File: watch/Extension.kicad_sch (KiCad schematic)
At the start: 1 part

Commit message: Add speaker
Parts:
- added LS801: Speaker, Same Sky:CMR-12062S-67, symbol Device:Speaker
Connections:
- net GND: now also M801.S113 (GND); no longer M801.S11 (GND)
- net Status: now also M801.S112 (Status); no longer M801.S114 (Status)
- net VHR: now also M801.S12 (+1V8_{HR}); no longer M801.S14 (+1V8_{HR})
- net VSYS: now also M801.S14 (V_{SYS}); no longer M801.S12 (V_{SYS})
- net ~{RESET_{HR}}: now also M801.S114 (~{RESET_{HR}}); no longer M801.S112 (~{RESET_{HR}})
- removed net SP_{N}: M801.S21 (SP_{N})
- removed net SP_{P}: M801.S23 (SP_{P})
- new net: LS801.2, M801.S11 (SP_{N})
- new net: LS801.1, M801.S13 (SP_{P})
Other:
- title: (none) -> Extension
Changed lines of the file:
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@@
 	(paper "A4")
 	(title_block
+		(title "Extension")
 		(date "2025-07-13")
 		(rev "${REVISION}")
@@
 	(wire
 		(pts
+			(xy 172.72 86.36) (xy 184.15 86.36)
+		)
+		(stroke
+			(width 0)
+			(type default)
+		)
+	)
+	(wire
+		(pts
 			(xy 152.4 111.76) (xy 152.4 110.49)
 		)
@@
 	(wire
 		(pts
-			(xy 172.72 86.36) (xy 173.99 86.36)
-		)
-		(stroke
-			(width 0)
-			(type default)
-		)
-	)
-	(wire
-		(pts
 			(xy 128.27 82.55) (xy 129.54 82.55)
 		)
@@
 	(wire
 		(pts
-			(xy 172.72 88.9) (xy 173.99 88.9)
+			(xy 172.72 88.9) (xy 184.15 88.9)
 		)
 		(stroke
@@
 		)
 	)
-	(hierarchical_label "SP_{P}"
-		(shape output)
-		(at 173.99 88.9 0)
-		(effects
-			(font
-				(size 1.27 1.27)
-			)
-			(justify left)
-		)
-	)
 	(hierarchical_label "VHR"
 		(shape input)
 		(at 148.59 63.5 90)
-		(effects
-			(font
-				(size 1.27 1.27)
-			)
-			(justify left)
-		)
-	)
-	(hierarchical_label "SP_{N}"
-		(shape output)
-		(at 173.99 86.36 0)
 		(effects
 			(font
@@
 		(pin "S210"
 		)
-		(pin "S23"
+		(pin "S113"
 		)
 		(pin "S114"
 		)
-		(pin "S21"
+		(pin "S13"
 		)
 		(instances
@@
 					(unit 1)
 				)
+			)
+		)
+	)
+	(symbol
+		(lib_id "Device:Speaker")
+		(at 189.23 86.36 0)
+		(unit 1)
+		(exclude_from_sim no)
+		(in_bom yes)
+		(on_board yes)
+		(dnp no)
+		(fields_autoplaced yes)
+		(property "Reference" "LS801"
+			(at 194.31 86.3599 0)
+			(effects
+				(font
+					(size 1.27 1.27)
+				)
+				(justify left)
+			)
+		)
+		(property "Value" "Speaker"
+			(at 194.31 88.8999 0)
+			(effects
+				(font
+					(size 1.27 1.27)
+				)
+				(justify left)
+			)
+		)
+		(property "Footprint" "Same Sky:CMR-12062S-67"
+			(at 189.23 91.44 0)
+			(effects
+				(font
+					(size 1.27 1.27)
+				)
+				(hide yes)
+			)
+		)
+		(property "Datasheet" "https://www.mouser.de/datasheet/3/6118/1/cmr_12062s_67.pdf"
+			(at 188.976 87.63 0)
+			(effects
+				(font
+					(size 1.27 1.27)
+				)
+				(hide yes)
+			)
+		)
+		(property "Description" "Speaker"
+			(at 189.23 86.36 0)
+			(effects
+				(font
+					(size 1.27 1.27)
+				)
+				(hide yes)
+			)
+		)
+		(property "manf" "Same Sky"
+			(at 189.23 86.36 0)
+			(effects
+				(font
+					(size 1.27 1.27)
+				)
+				(hide yes)
+			)
+		)
+		(property "manf#" "CMR-12062S-67"
+			(at 189.23 86.36 0)
+			(effects
+				(font
+					(size 1.27 1.27)
+				)
+				(hide yes)
+			)
+		)
+		(property "mouser#" "490-CMR-12062S-67"
+			(at 189.23 86.36 0)
+			(effects
+				(font
+					(size 1.27 1.27)
+				)
+				(hide yes)
+			)
+		)
+		(property "CONFIG" ""
+			(at 189.23 86.36 0)
+			(effects
+				(font
+					(size 1.27 1.27)
+				)
+				(hide yes)
+			)
+		)
+		(pin "1"
+		)
+		(pin "2"
+		)
+		(instances
+			(project "ZSWatch-Watch"
+				(path "/d5742f03-3b1a-42e5-a384-018bd4b919aa/c5103ceb-5325-4a84-a025-9638a412984e/ecef31af-e159-4d83-89cb-c5b343e56438"
+					(reference "LS801")
+					(unit 1)
+				)

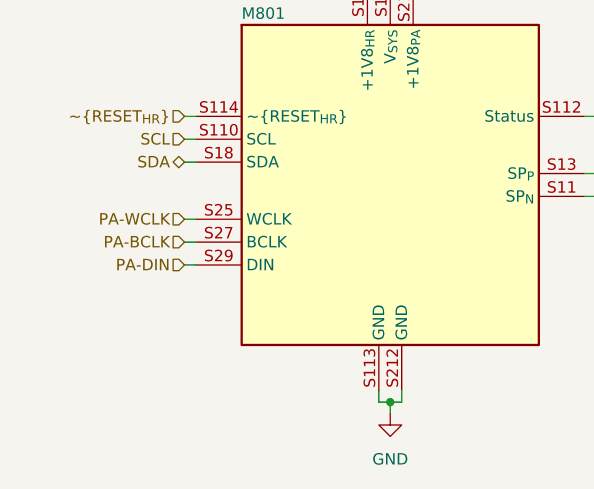
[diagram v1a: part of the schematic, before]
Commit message: Fix wrong Extension footprint
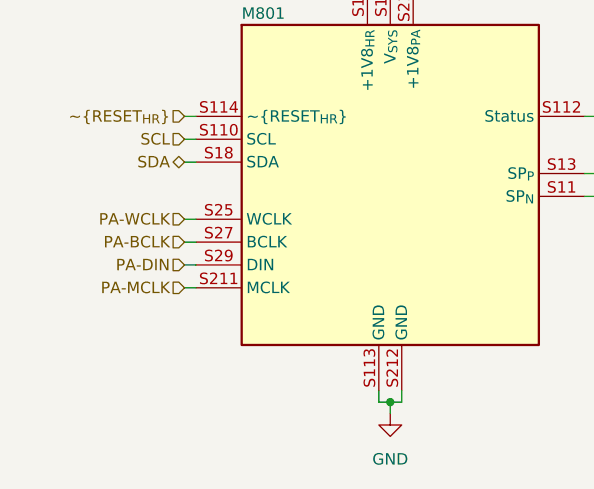
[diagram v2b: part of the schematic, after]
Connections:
- new net PA-MCLK: M801.S211 (MCLK)
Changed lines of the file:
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@@
+	(wire
+		(pts
+			(xy 128.27 99.06) (xy 129.54 99.06)
+		)
+		(stroke
+			(width 0)
+			(type default)
+		)
+	)
 	(wire
 		(pts
@@
 			(width 0)
 			(type default)
+		)
+	)
+	(hierarchical_label "PA-MCLK"
+		(shape input)
+		(at 128.27 99.06 180)
+		(effects
+			(font
+				(size 1.27 1.27)
+			)
+			(justify right)
 		)
 	)
@@
 		(pin "S13"
 		)
+		(pin "S211"
+		)
 		(instances

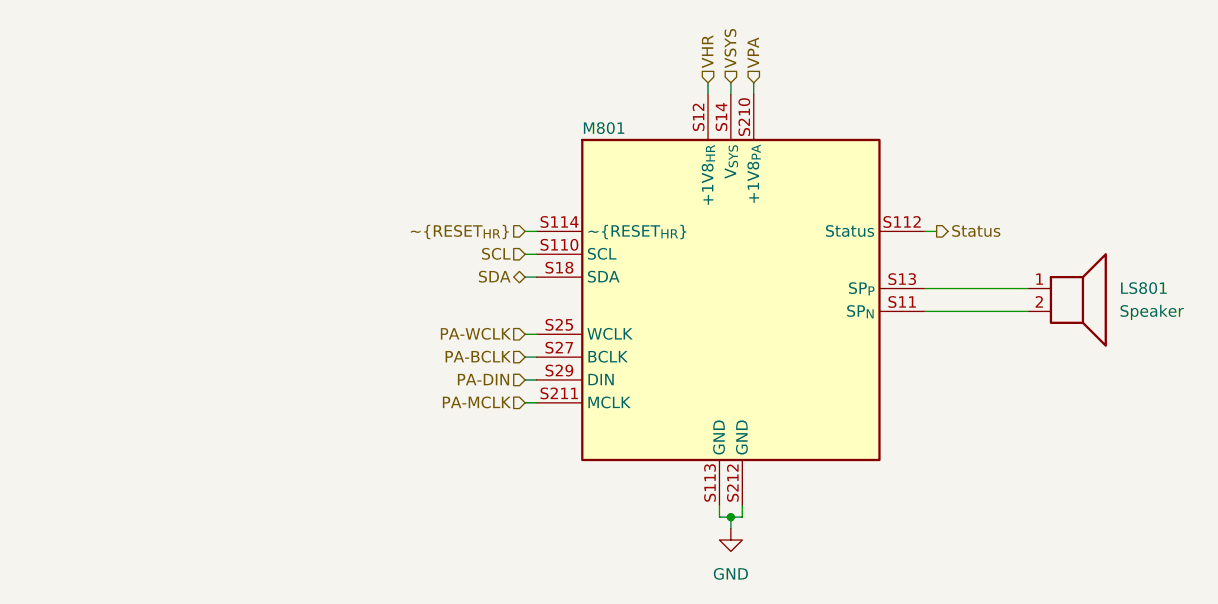
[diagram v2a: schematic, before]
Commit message: New battery connector
- Add CI/CD workflow to check for changelog updates on pull requests

Signed-off-by: Daniel Kampert <DanielKampert|kampis-elektroecke.de>
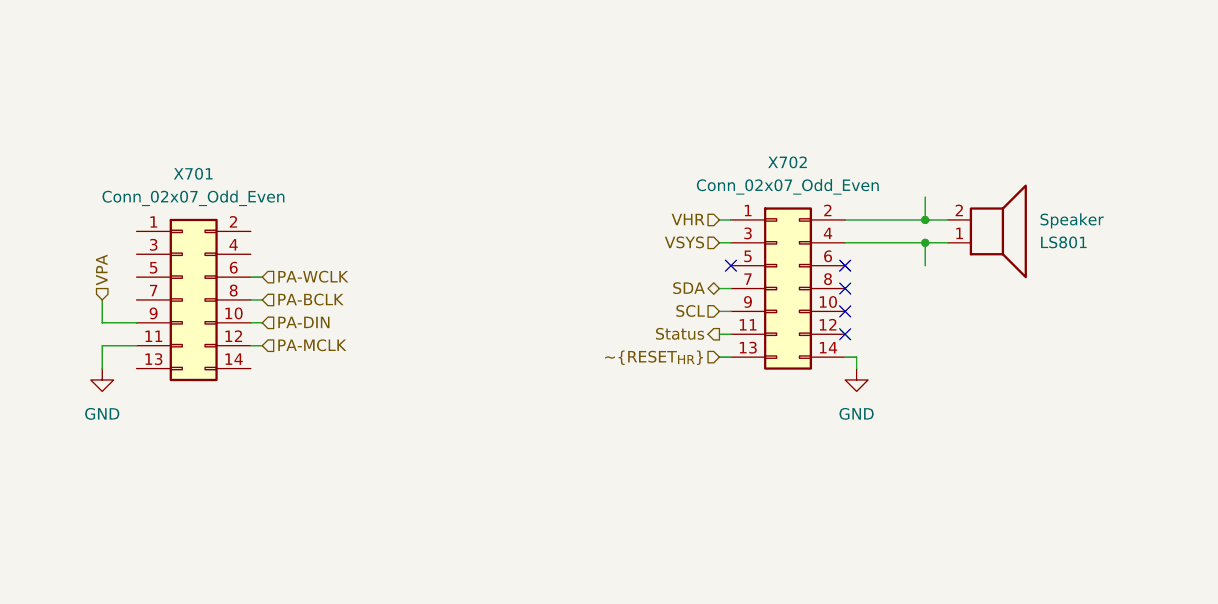
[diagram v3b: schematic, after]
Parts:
- removed M801: ~, ZSWatch:Extension, symbol ZSWatch:Extension
- added X701, X702: Conn_02x07_Odd_Even, Amphenol:101P014FB110, symbol Connector_Generic:Conn_02x07_Odd_Even
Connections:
- net GND: now also X701.11 (Pin_11), X702.14 (Pin_14)
- net PA-BCLK: now also X701.8 (Pin_8)
- net PA-DIN: now also X701.10 (Pin_10)
- net PA-MCLK: now also X701.12 (Pin_12)
- net PA-WCLK: now also X701.6 (Pin_6)
- net SCL: now also X702.9 (Pin_9)
- net SDA: now also X702.7 (Pin_7)
- net Status: now also X702.11 (Pin_11)
- net VHR: now also X702.1 (Pin_1)
- net VPA: now also X701.9 (Pin_9)
- net VSYS: now also X702.3 (Pin_3)
- net ~{RESET_{HR}}: now also X702.13 (Pin_13)
- net at LS801.2: now also X702.2 (Pin_2)
- net at LS801.1: now also X702.4 (Pin_4)
- no-connect marks 0 -> 5
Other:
- moved on the sheet: LS801

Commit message: Replace wrong extension connectors
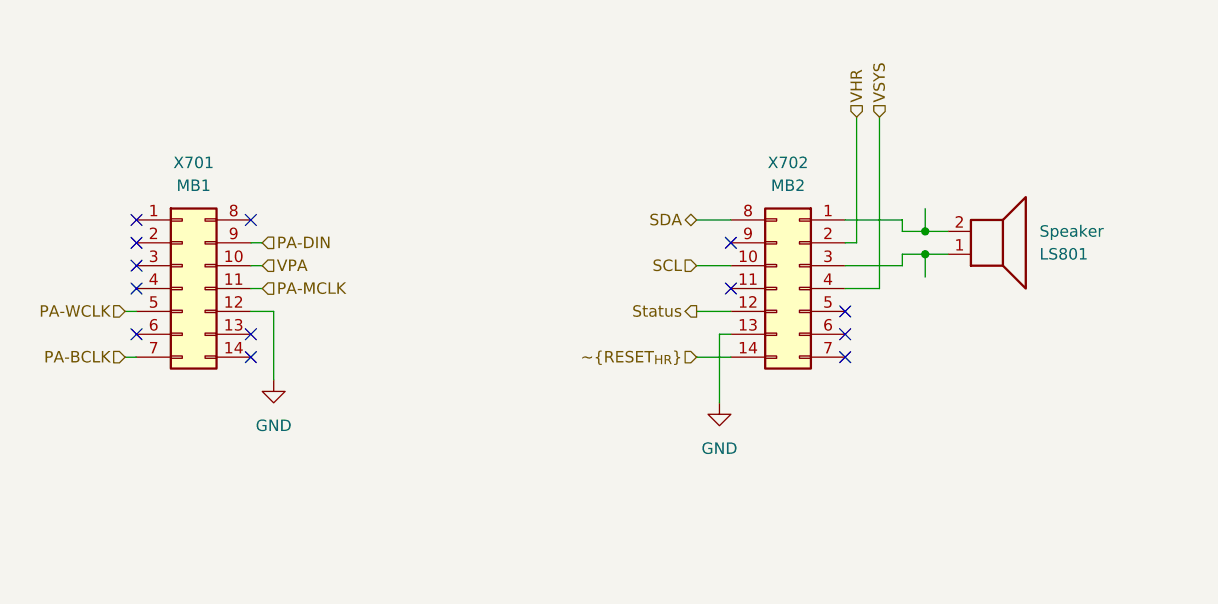
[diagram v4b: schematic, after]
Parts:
- X701: value Conn_02x07_Odd_Even -> MB1; footprint Amphenol:101P014FB110 -> Amphenol:101R014FB110; symbol Connector_Generic:Conn_02x07_Odd_Even -> Connector_Generic:Conn_02x07_Top_Bottom; manf (none) -> Amphenol Aorora; manf# (none) -> 101R014FB110; mouser# (none) -> 649-101R014FB110
- X702: value Conn_02x07_Odd_Even -> MB2; footprint Amphenol:101P014FB110 -> Amphenol:101R014FB110; symbol Connector_Generic:Conn_02x07_Odd_Even -> Connector_Generic:Conn_02x07_Top_Bottom; manf (none) -> Amphenol Aorora; manf# (none) -> 101R014FB110; mouser# (none) -> 649-101R014FB110
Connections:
- net GND: now also X701.12 (Pin_12), X702.13 (Pin_13); no longer X701.11 (Pin_11), X702.14 (Pin_14)
- net PA-BCLK: now also X701.7 (Pin_7); no longer X701.8 (Pin_8)
- net PA-DIN: now also X701.9 (Pin_9); no longer X701.10 (Pin_10)
- net PA-MCLK: now also X701.11 (Pin_11); no longer X701.12 (Pin_12)
- net PA-WCLK: now also X701.5 (Pin_5); no longer X701.6 (Pin_6)
- net SCL: now also X702.10 (Pin_10); no longer X702.9 (Pin_9)
- net SDA: now also X702.8 (Pin_8); no longer X702.7 (Pin_7)
- net Status: now also X702.12 (Pin_12); no longer X702.11 (Pin_11)
- net VHR: now also X702.2 (Pin_2); no longer X702.1 (Pin_1)
- net VPA: now also X701.10 (Pin_10); no longer X701.9 (Pin_9)
- net VSYS: now also X702.4 (Pin_4); no longer X702.3 (Pin_3)
- net ~{RESET_{HR}}: now also X702.14 (Pin_14); no longer X702.13 (Pin_13)
- net at LS801.2: now also X702.1 (Pin_1); no longer X702.2 (Pin_2)
- net at LS801.1: now also X702.3 (Pin_3); no longer X702.4 (Pin_4)
- no-connect marks 5 -> 13
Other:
- moved on the sheet: LS801, X701
